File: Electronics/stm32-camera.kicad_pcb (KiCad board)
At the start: 4 copper layers, 36 x 36 mm, 61 parts, among them CON1 MOLEX_47309-2651, P1 CONN_01X08, P2 MOLEX_PICO_PTH_VERT_2_WAY, P3 CONN_01X03, Q1 TEMT7000X01, SW1 B3U-1000P_SPST-NO_SMD, U1 STM32F429VET6, U2 AP2210K-ADJ, U3 AP2210K-ADJ, U4 AP2210K-ADJ, U5 OV02640-VL9A, X1 CSTCE16M0V53A, X2 SWD

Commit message: Continued messing around with layout
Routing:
- net GND: track 52.0 -> 58.5 mm, vias 21 -> 23
- net +2.8V: track 1.66 -> 6.00 mm
- net +1.3V: track 0.89 -> 5.24 mm
- net +3.3V: track 41.1 -> 44.8 mm

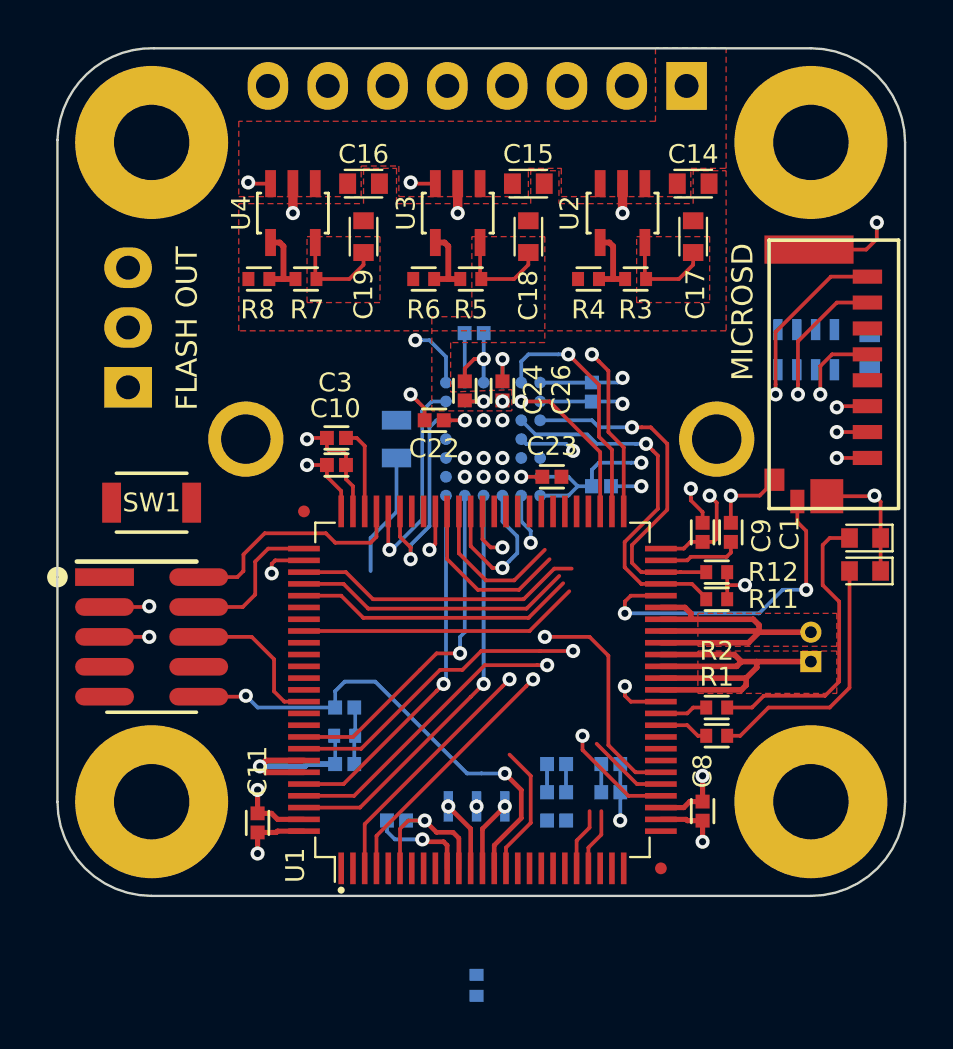
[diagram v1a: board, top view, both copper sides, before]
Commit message: Routed SD lines and repositioned parts. Re-pinned SD pullup array. Button connected to micro, etc.
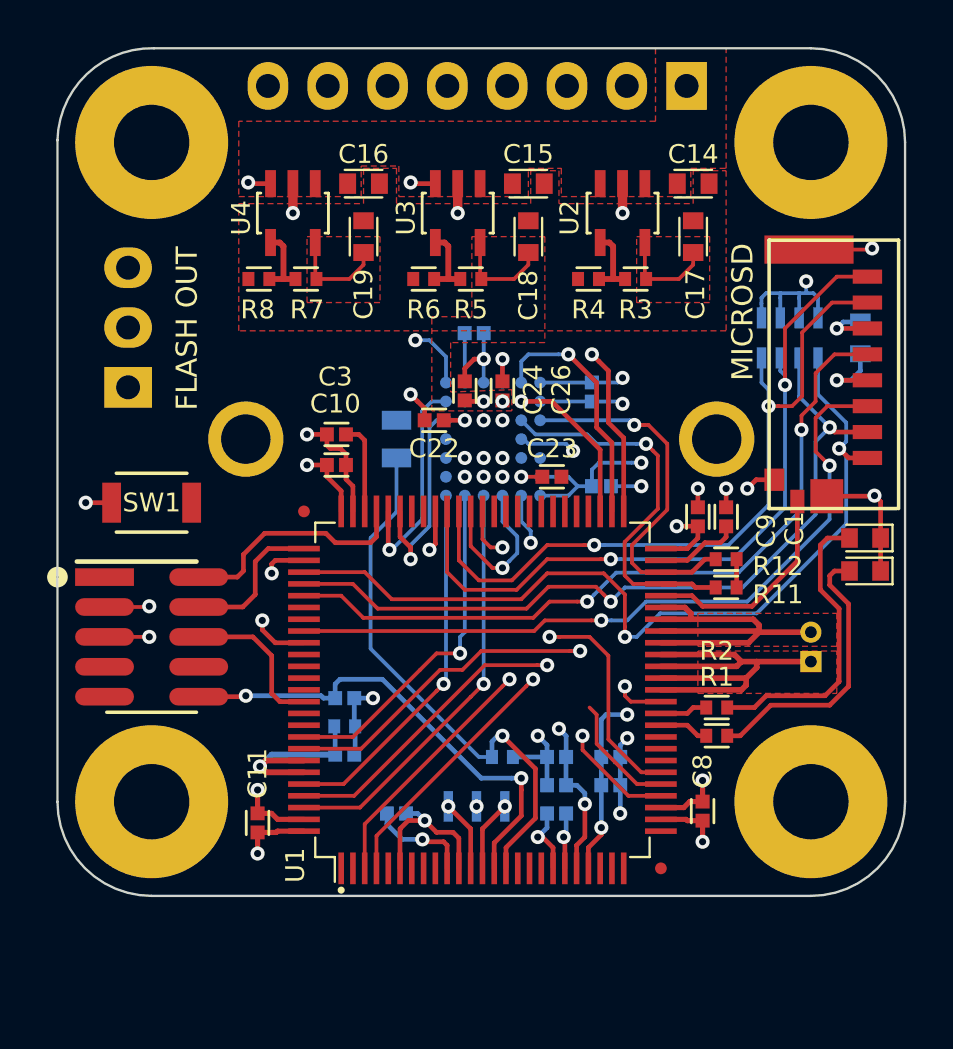
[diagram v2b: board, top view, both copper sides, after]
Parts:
- moved R10 9.76 mm to (118.9, 130.1), turned to 0 degrees
- moved R9 0.86 mm to (131.1, 112.3)
- moved C9 0.69 mm to (127.2, 119.9)
- moved C1 0.69 mm to (128.4, 119.9)
- moved R12 0.68 mm to (128.4, 121.7)
- moved C20 0.64 mm to (134.1, 112.3)
- moved R11 0.64 mm to (128.4, 122.9)
- moved C2 0.40 mm to (112.2, 127.6)
- moved C28 0.40 mm to (112.2, 130.0)
- moved R13 0.40 mm to (112.2, 128.8)
- moved C12 0.30 mm to (121.2, 130.1)
- moved C5 0.30 mm to (123.5, 130.1)
- moved C6 0.30 mm to (114.4, 132.5)
- moved C7 0.30 mm to (121.2, 132.5)
- moved C13 0.30 mm to (121.2, 131.3)
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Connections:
- R9 pad 5: MICROSD_D1 -> MICROSD_D2
- R9 pad 6: MICROSD_D0 -> MICROSD_D3
- R9 pad 7: MICROSD_D3 -> MICROSD_D1
- R9 pad 8: MICROSD_D2 -> MICROSD_D0
- SW1 pad 1: (no net) -> BUTTON0
- SW1 pad 2: (no net) -> GND
- U1 pad 84: (no net) -> BUTTON0
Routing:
- net MICROSD_D2: track 13.7 -> 37.3 mm, vias 1 -> 2
- net MICROSD_D3: track 13.2 -> 33.5 mm, vias 1 -> 2
- net MICROSD_D0: track 12.3 -> 30.9 mm, vias 1 -> 2
- net MICROSD_CMD: track 13.3 -> 31.2 mm, vias 1 -> 2
- net +3.3V: track 44.8 -> 62.3 mm, vias 8 -> 14
- net MICROSD_D1: track 15.0 -> 31.9 mm, vias 1 -> 2
- net MICROSD_CK: track 15.4 -> 32.3 mm, vias 1 -> 2
- net AMBIENT_LIGHT: track 10.9 -> 23.5 mm, vias 0 -> 1
- net GND: track 58.5 -> 65.7 mm, vias 23 -> 30
- net PWR_EN: track 10.8 -> 3.87 mm
- net MICROSD_DETECT: track 14.2 -> 9.30 mm, vias 2 -> 0
- net BUTTON0: track 0.00 -> 2.40 mm, vias 0 -> 1
- net FLASH_DAC: track 3.44 -> 5.10 mm
- net Net-(D1-PadA): track 11.0 -> 12.0 mm
- net SIO_D: track 14.8 -> 15.4 mm

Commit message: Routing, pours and cosmetic changes. Many general improvements to PCB.
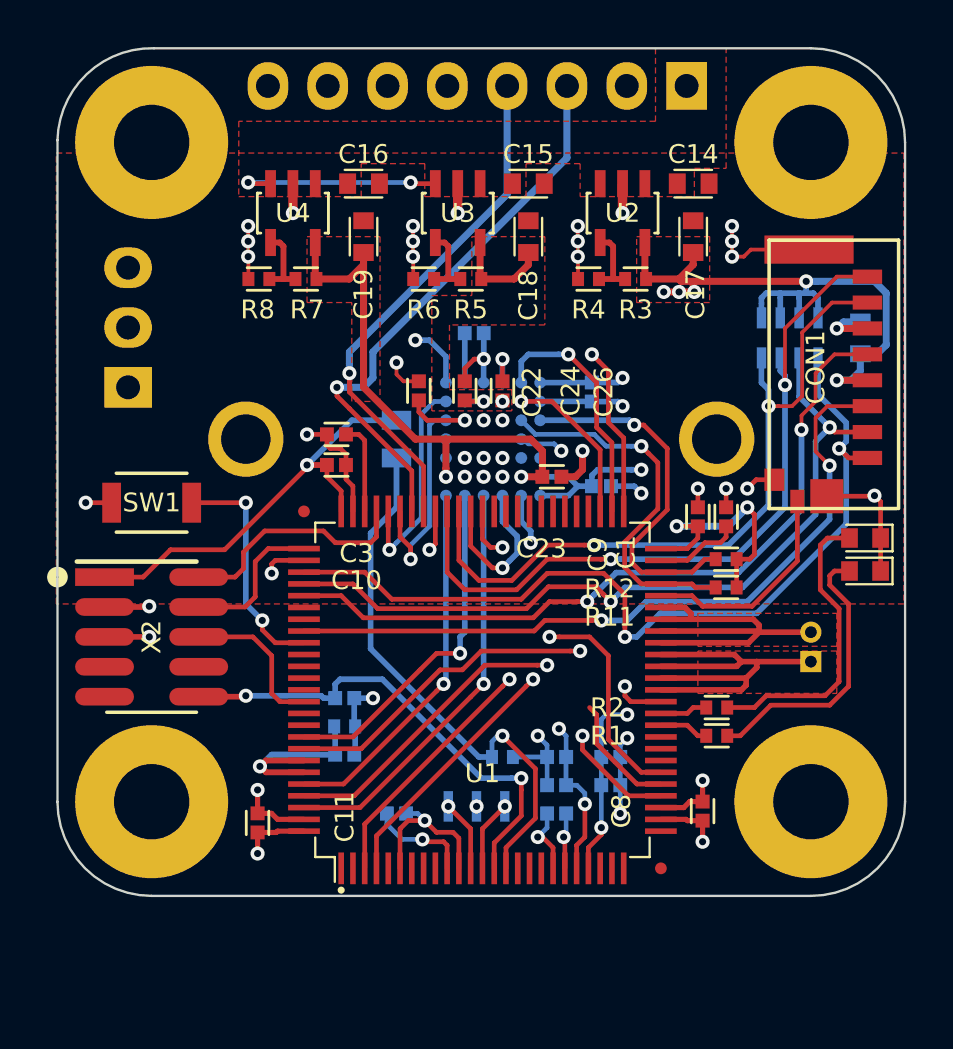
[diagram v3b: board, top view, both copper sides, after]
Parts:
- moved C22 1.41 mm to (115.3, 114.5), turned to 90 degrees
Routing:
- net +3.3V: track 62.3 -> 97.9 mm, vias 14 -> 18
- net UART_RX: track 0.00 -> 24.1 mm, vias 0 -> 1
- net UART_TX: track 0.00 -> 22.2 mm, vias 0 -> 1
- net +1.3V: track 5.24 -> 22.4 mm, vias 1 -> 2
- net GND: track 65.7 -> 76.6 mm, vias 30 -> 42
- net BUTTON0: track 2.40 -> 9.99 mm, vias 1 -> 2
- net PWR_EN: track 3.87 -> 10.8 mm
- net Net-(C22-Pad1): track 0.89 -> 2.59 mm
- net D4: track 21.7 -> 22.7 mm
- net XCLK: track 9.06 -> 9.71 mm
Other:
- board text added: "Board Manufacture Information 1.6mm FR4, 1oz (35um) copper 4 Layer ENIG Surface Finish Black Soldermask White Silkscreen Min Track: 0.2mm Min Clearance: 0.2mm Min Via: 0.3mm"
- board text removed: "Board Manufacture Information 1.6mm FR4, 1oz (35um) copper ? Layer ENIG Surface Finish Black Soldermask White Silkscreen Min Track: 0.16mm Min Clearance: 0.16mm Min Via: 0.3mm"
- board text removed: "FLASH OUT"
- board text removed: "MICROSD"

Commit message: Routing changes and changed DRC width. Increased min track on board to .2mm. Fixed many DRC errors.
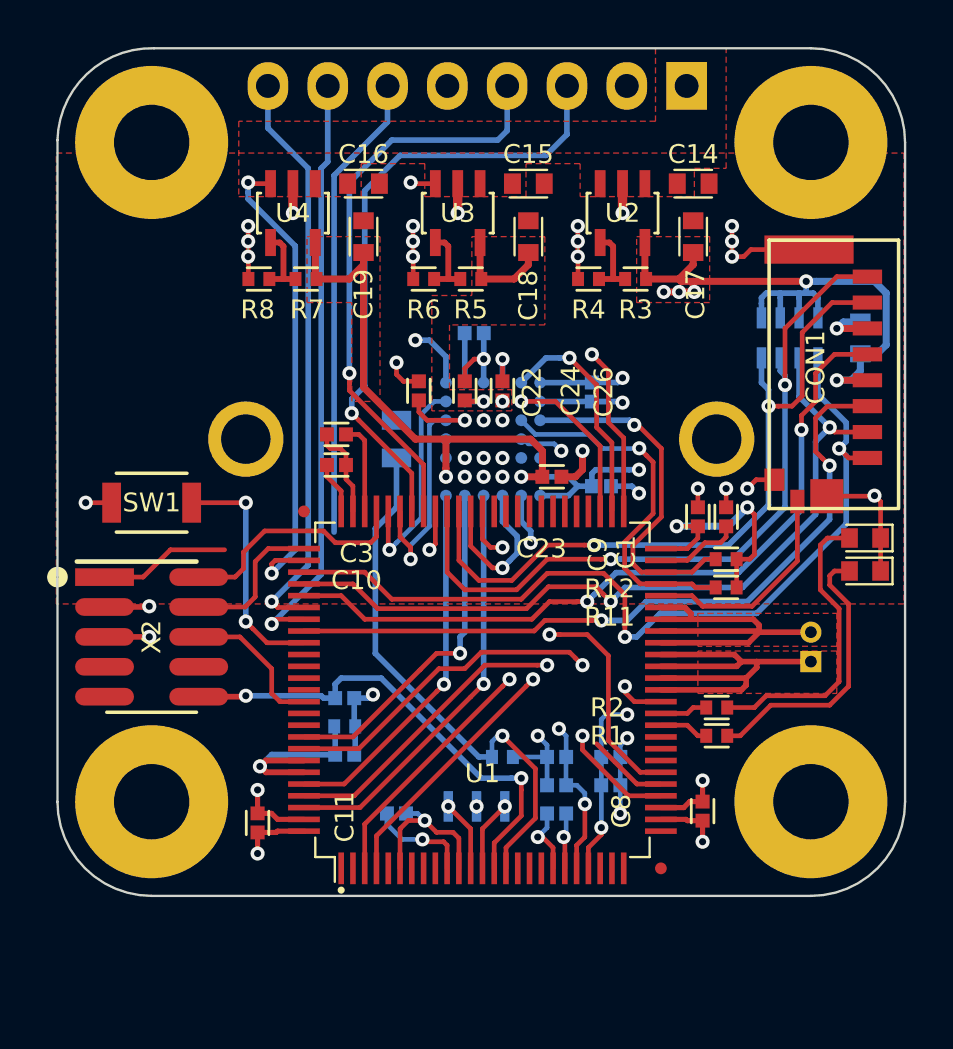
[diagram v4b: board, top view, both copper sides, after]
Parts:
- removed P3: CONN_01X03, Applidyne_Header:Pin_Header_Straight_1x03
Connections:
- P1 pad 5: (no net) -> GND
- P1 pad 6: (no net) -> FLASH_DAC
- P1 pad 7: (no net) -> EXP_0
- P1 pad 8: (no net) -> EXP_1
- U1 pad 1: (no net) -> Net-(U1-Pad1)
- U1 pad 16: (no net) -> Net-(U1-Pad16)
- U1 pad 17: (no net) -> Net-(U1-Pad17)
- U1 pad 18: (no net) -> Net-(U1-Pad18)
- U1 pad 2: (no net) -> Net-(U1-Pad2)
- U1 pad 23: (no net) -> Net-(U1-Pad23)
- U1 pad 24: (no net) -> Net-(U1-Pad24)
- U1 pad 25: (no net) -> Net-(U1-Pad25)
- U1 pad 26: (no net) -> Net-(U1-Pad26)
- U1 pad 32: (no net) -> Net-(U1-Pad32)
- U1 pad 33: (no net) -> Net-(U1-Pad33)
- U1 pad 34: (no net) -> Net-(U1-Pad34)
- U1 pad 5: (no net) -> Net-(U1-Pad5)
- U1 pad 54: (no net) -> Net-(U1-Pad54)
- U1 pad 55: (no net) -> Net-(U1-Pad55)
- U1 pad 56: (no net) -> Net-(U1-Pad56)
- U1 pad 57: (no net) -> Net-(U1-Pad57)
- U1 pad 58: (no net) -> Net-(U1-Pad58)
- U1 pad 59: (no net) -> Net-(U1-Pad59)
- U1 pad 60: (no net) -> Net-(U1-Pad60)
- U1 pad 61: (no net) -> Net-(U1-Pad61)
- U1 pad 62: (no net) -> Net-(U1-Pad62)
- U1 pad 7: (no net) -> Net-(U1-Pad7)
- U1 pad 8: (no net) -> Net-(U1-Pad8)
- U1 pad 81: (no net) -> EXP_1
- U1 pad 82: (no net) -> EXP_0
- U1 pad 85: (no net) -> Net-(U1-Pad85)
- U1 pad 86: (no net) -> Net-(U1-Pad86)
- U1 pad 87: (no net) -> Net-(U1-Pad87)
- U1 pad 88: (no net) -> Net-(U1-Pad88)
- U1 pad 9: (no net) -> Net-(U1-Pad9)
- U1 pad 90: (no net) -> Net-(U1-Pad90)
- U1 pad 91: (no net) -> Net-(U1-Pad91)
- U5 pad D6: (no net) -> Net-(U5-PadD6)
- U5 pad E1: (no net) -> Net-(U5-PadE1)
- U5 pad E2: (no net) -> Net-(U5-PadE2)
- X2 pad 7: (no net) -> Net-(X2-Pad7)
- X2 pad 8: (no net) -> Net-(X2-Pad8)
- X2 pad 9: (no net) -> Net-(X2-Pad9)
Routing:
- net EXP_0: track 0.00 -> 25.3 mm, vias 0 -> 1
- net EXP_1: track 0.00 -> 24.7 mm, vias 0 -> 1
- net FLASH_DAC: track 5.10 -> 23.3 mm
- net PWR_EN: track 10.8 -> 28.6 mm
- net +3.3V: track 97.9 -> 87.3 mm, vias 18 -> 17
- net UART_TX: track 22.2 -> 24.8 mm
- net UART_RX: track 24.1 -> 26.5 mm
- net GND: track 76.6 -> 75.6 mm, vias 42 -> 41
- net VSYNC: track 24.2 -> 25.1 mm
- net EXPSTB: track 10.5 -> 9.75 mm
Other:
- net class Default: clearance 0.15 -> 0.18; trace_width 0.16 -> 0.2
- rule trace_clearance: 0.15 -> 0.18
- rule trace_min: 0.16 -> 0.2

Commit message: Everything routed. Silkscreen cleanups. Fixed all DRC warnings.
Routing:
- net +3.3V: track 87.3 -> 188.5 mm, vias 17 -> 18
- net FLASH_DAC: track 23.3 -> 42.1 mm, vias 0 -> 3
- net GND: track 75.6 -> 84.8 mm
- net UART_TX: track 24.8 -> 23.9 mm
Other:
- board text added: "A"
- board text added: "Board Manufacture Information 1.6mm FR4, 1oz (35um) copper 4 Layer ENIG Surface Finish Black Soldermask White Silkscreen Min Track: 0.2mm Min Clearance: 0.2mm Min Via Drill: 0.3mm"
- board text added: "E0"
- board text added: "E1"
- board text added: "GND"
- board text added: "RX"
- board text added: "TX"
- board text added: "VIN"
- board text removed: "Board Manufacture Information 1.6mm FR4, 1oz (35um) copper 4 Layer ENIG Surface Finish Black Soldermask White Silkscreen Min Track: 0.2mm Min Clearance: 0.2mm Min Via: 0.3mm"

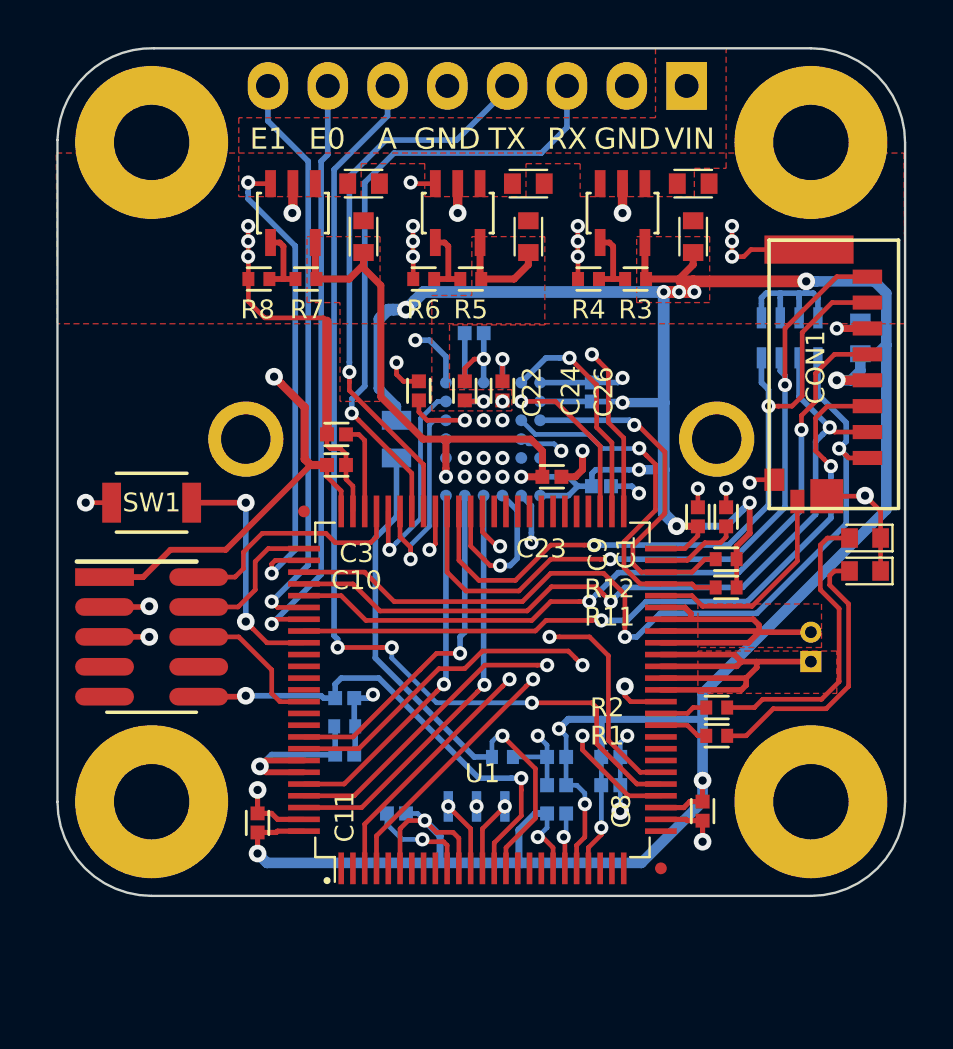
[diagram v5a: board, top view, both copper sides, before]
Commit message: Added RC snubber to address #5.
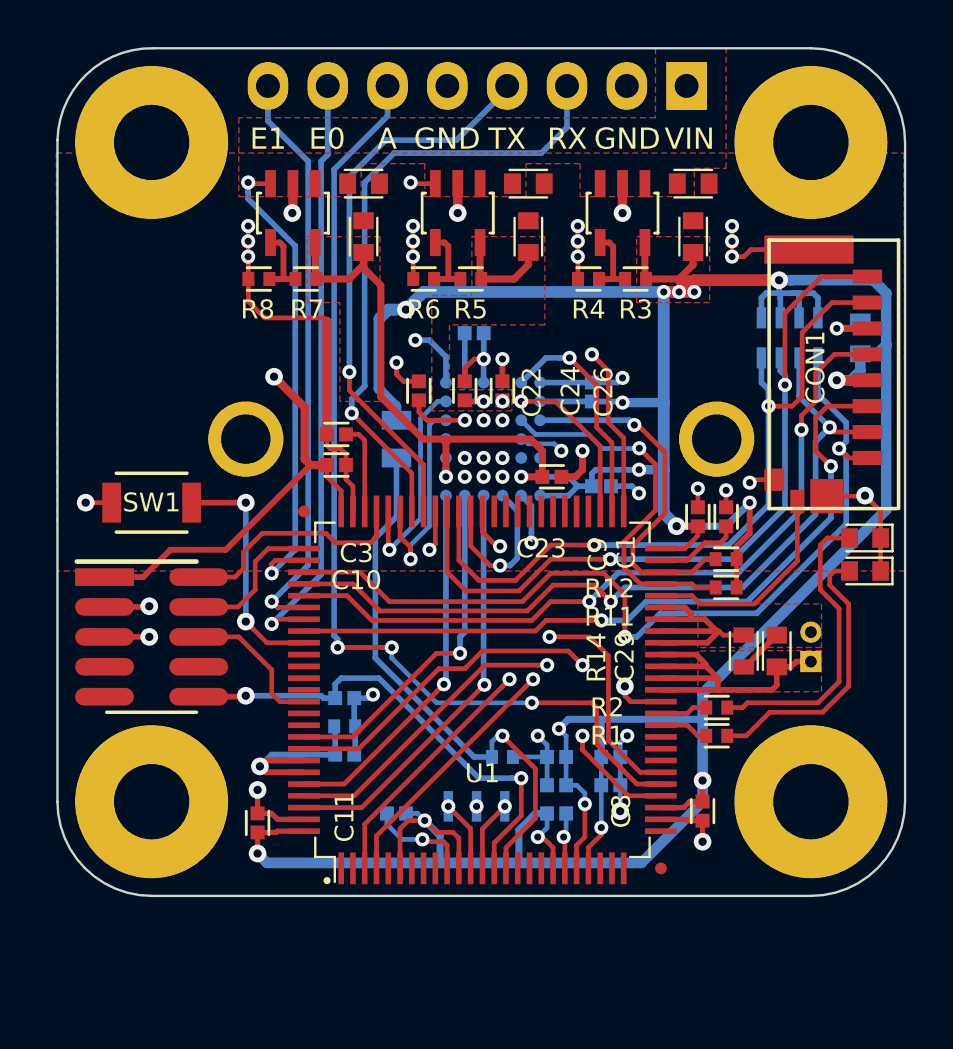
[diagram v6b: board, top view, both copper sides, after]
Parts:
- added C29: 100NF_X7R_1608M, Applidyne_Capacitor:CAPC1608X90L, F.Cu at (130.6, 125.6)
- added R14: 100R_1608M, Applidyne_Resistor:RESC1608X50L, F.Cu at (129.2, 125.6)
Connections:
- U1 pad 1: Net-(U1-Pad1) -> (no net)
- U1 pad 16: Net-(U1-Pad16) -> (no net)
- U1 pad 17: Net-(U1-Pad17) -> (no net)
- U1 pad 18: Net-(U1-Pad18) -> (no net)
- U1 pad 2: Net-(U1-Pad2) -> (no net)
- U1 pad 23: Net-(U1-Pad23) -> (no net)
- U1 pad 24: Net-(U1-Pad24) -> (no net)
- U1 pad 25: Net-(U1-Pad25) -> (no net)
- U1 pad 26: Net-(U1-Pad26) -> (no net)
- U1 pad 32: Net-(U1-Pad32) -> (no net)
- U1 pad 33: Net-(U1-Pad33) -> (no net)
- U1 pad 34: Net-(U1-Pad34) -> (no net)
- U1 pad 5: Net-(U1-Pad5) -> (no net)
- U1 pad 54: Net-(U1-Pad54) -> (no net)
- U1 pad 55: Net-(U1-Pad55) -> (no net)
- U1 pad 56: Net-(U1-Pad56) -> (no net)
- U1 pad 57: Net-(U1-Pad57) -> (no net)
- U1 pad 58: Net-(U1-Pad58) -> (no net)
- U1 pad 59: Net-(U1-Pad59) -> (no net)
- U1 pad 60: Net-(U1-Pad60) -> (no net)
- U1 pad 61: Net-(U1-Pad61) -> (no net)
- U1 pad 62: Net-(U1-Pad62) -> (no net)
- U1 pad 7: Net-(U1-Pad7) -> (no net)
- U1 pad 8: Net-(U1-Pad8) -> (no net)
- U1 pad 85: Net-(U1-Pad85) -> (no net)
- U1 pad 86: Net-(U1-Pad86) -> (no net)
- U1 pad 87: Net-(U1-Pad87) -> (no net)
- U1 pad 88: Net-(U1-Pad88) -> (no net)
- U1 pad 9: Net-(U1-Pad9) -> (no net)
- U1 pad 90: Net-(U1-Pad90) -> (no net)
- U1 pad 91: Net-(U1-Pad91) -> (no net)
- U5 pad D6: Net-(U5-PadD6) -> (no net)
- U5 pad E1: Net-(U5-PadE1) -> (no net)
- U5 pad E2: Net-(U5-PadE2) -> (no net)
- X2 pad 7: Net-(X2-Pad7) -> (no net)
- X2 pad 8: Net-(X2-Pad8) -> (no net)
- X2 pad 9: Net-(X2-Pad9) -> (no net)
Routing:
- net IRCUT_B: track 16.9 -> 10.5 mm
- net IRCUT_A: track 18.5 -> 15.0 mm
- net Net-(C29-Pad2): track 0.00 -> 1.96 mm

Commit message: Final silkscreen pass. Pin labels and branding are negative on soldermask. Let that gold shine through. Closes #6.
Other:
- board text added: "1.0.0 2017 Scott Rapson"
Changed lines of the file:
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@@
     (area 89.900001 93.54 208.228571 138.797143)
     (thickness 1.6)
-    (drawings 19)
+    (drawings 20)
     (tracks 901)
     (zones 0)
@@
     )
   )
-  (gr_text E1 (at 108.95 103.85) (layer F.SilkS)
+  (gr_text "1.0.0 2017\nScott Rapson\n" (at 102.975 108.15 270) (layer F.Mask)
+    (effects (font (size 0.9 0.9) (thickness 0.14)) (justify left))
+  )
+  (gr_text E1 (at 108.95 103.85) (layer F.Mask)
     (effects (font (size 0.9 0.9) (thickness 0.14)))
   )
-  (gr_text E0 (at 111.45 103.85) (layer F.SilkS)
+  (gr_text E0 (at 111.45 103.85) (layer F.Mask)
     (effects (font (size 0.9 0.9) (thickness 0.14)))
   )
-  (gr_text A (at 114 103.85) (layer F.SilkS)
+  (gr_text A (at 114 103.85) (layer F.Mask)
     (effects (font (size 0.9 0.9) (thickness 0.14)))
   )
-  (gr_text GND (at 116.55 103.85) (layer F.SilkS)
+  (gr_text GND (at 116.55 103.85) (layer F.Mask)
     (effects (font (size 0.9 0.9) (thickness 0.14)))
   )
-  (gr_text VIN (at 126.85 103.85) (layer F.SilkS)
+  (gr_text VIN (at 126.85 103.85) (layer F.Mask)
     (effects (font (size 0.9 0.9) (thickness 0.14)))
   )
-  (gr_text TX (at 119.1 103.85) (layer F.SilkS)
+  (gr_text TX (at 119.1 103.85) (layer F.Mask)
     (effects (font (size 0.9 0.9) (thickness 0.14)))
   )
-  (gr_text RX (at 121.65 103.85) (layer F.SilkS)
+  (gr_text RX (at 121.65 103.85) (layer F.Mask)
     (effects (font (size 0.9 0.9) (thickness 0.14)))
   )
-  (gr_text GND (at 124.2 103.85) (layer F.SilkS)
+  (gr_text GND (at 124.2 103.85) (layer F.Mask)
     (effects (font (size 0.9 0.9) (thickness 0.14)))
   )
